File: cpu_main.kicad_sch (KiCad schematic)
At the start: 18 parts, among them Q1 9018G, U1 Z80, U2 74LS244, U21 2764, U3 74LS257, U4 74LS257, U5 74LS00, U6 27128, U7 27128/27256, U8 GA1, U9 74LS273

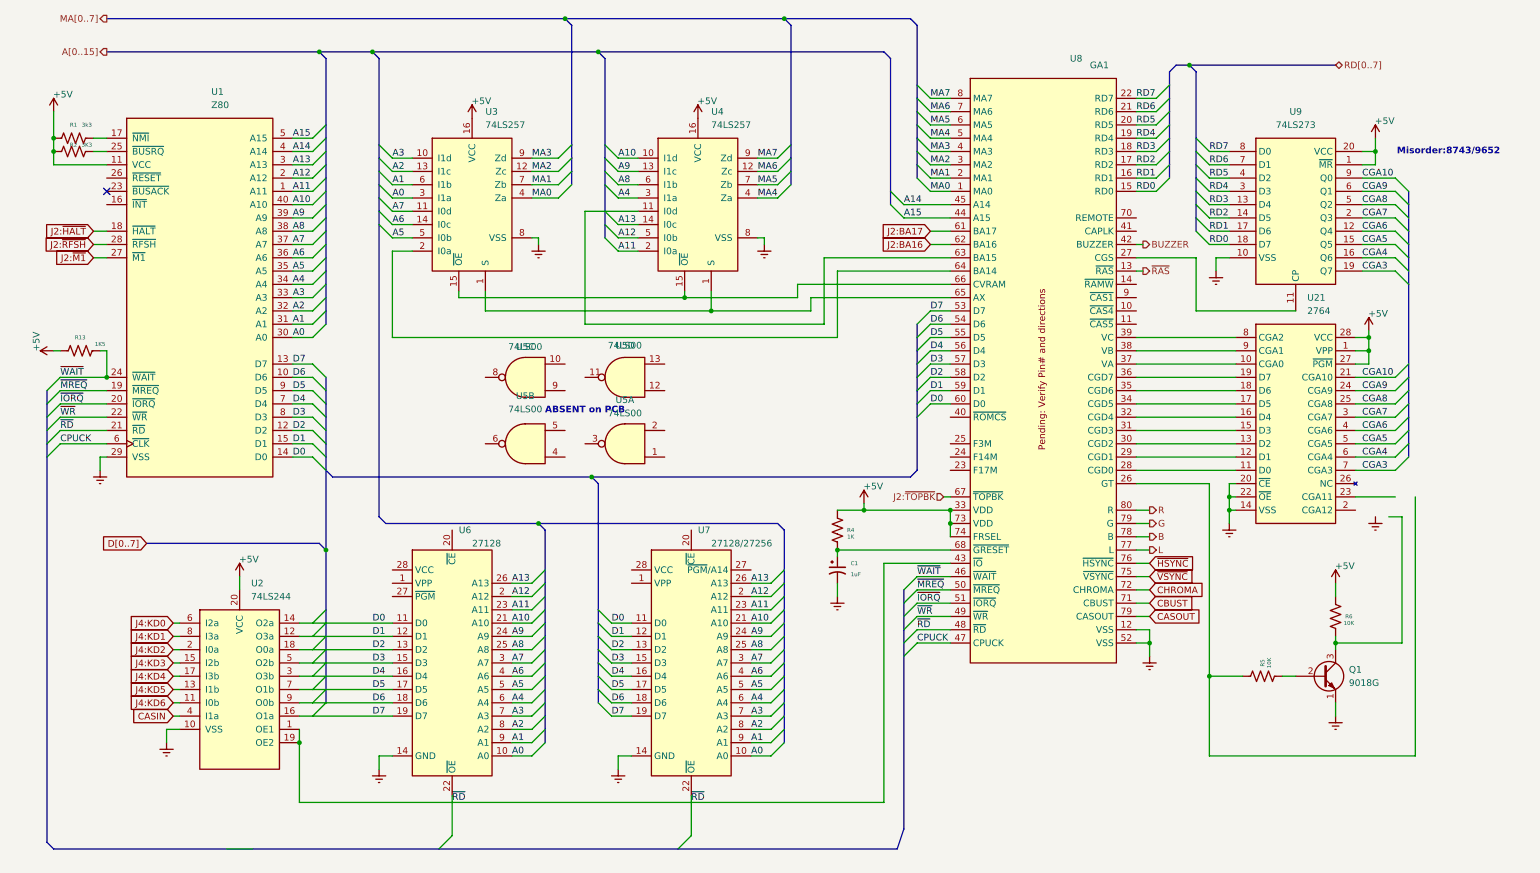
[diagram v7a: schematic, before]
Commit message: More updates on Top and Main diagrams
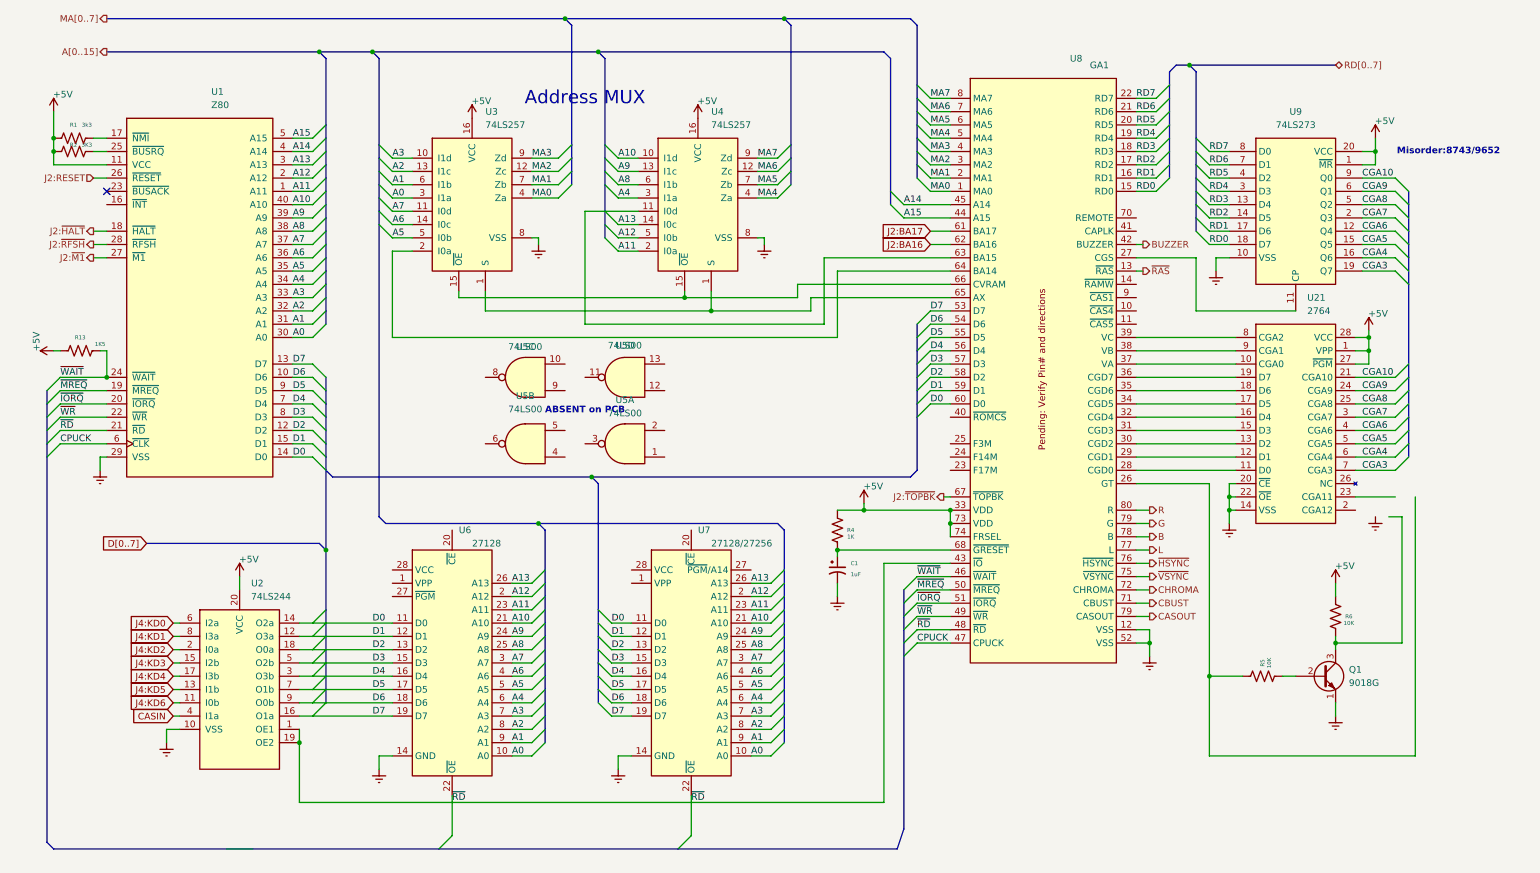
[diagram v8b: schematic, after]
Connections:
- net J2:RESET: now reaches U1.26 (~{RESET})
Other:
- note added: "Address MUX"
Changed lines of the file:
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@@
 		)
 	)
+	(wire
+		(pts
+			(xy 25.4 46.99) (xy 27.94 46.99)
+		)
+		(stroke
+			(width 0)
+			(type default)
+		)
+	)
 	(bus
 		(pts
@@
 		)
 	)
+	(text "Address MUX"
+		(exclude_from_sim no)
+		(at 119.38 31.75 0)
+		(effects
+			(font
+				(size 2.54 2.54)
+			)
+		)
+	)
 	(text "Misorder:8743/9652"
 		(exclude_from_sim no)
@@
 		)
 	)
-	(global_label "CBUST"
+	(global_label "D[0..7]"
 		(shape input)
-		(at 227.33 128.27 0)
+		(at 35.56 116.84 180)
 		(fields_autoplaced yes)
 		(effects
@@
 				(size 1.27 1.27)
 			)
-			(justify left)
+			(justify right)
 		)
 		(property "Intersheetrefs" "${INTERSHEET_REFS}"
-			(at 236.3628 128.27 0)
+			(at 25.9828 116.84 0)
 			(effects
 				(font
 					(size 1.27 1.27)
 				)
-				(justify left)
+				(justify right)
 				(hide yes)
 			)
 		)
 	)
-	(global_label "D[0..7]"
+	(global_label "J4:KD3"
 		(shape input)
-		(at 35.56 116.84 180)
+		(at 40.64 139.7 180)
 		(fields_autoplaced yes)
 		(effects
@@
 		)
 		(property "Intersheetrefs" "${INTERSHEET_REFS}"
-			(at 25.9828 116.84 0)
+			(at 31.1234 139.7 0)
 			(effects
 				(font
@@
 		)
 	)
-	(global_label "~{VSYNC}"
+	(global_label "J2:BA17"
 		(shape input)
-		(at 227.33 123.19 0)
+		(at 185.42 57.15 180)
 		(fields_autoplaced yes)
 		(effects
@@
 				(size 1.27 1.27)
 			)
-			(justify left)
+			(justify right)
 		)
 		(property "Intersheetrefs" "${INTERSHEET_REFS}"
-			(at 236.3024 123.19 0)
+			(at 174.8753 57.15 0)
 			(effects
 				(font
 					(size 1.27 1.27)
 				)
-				(justify left)
+				(justify right)
 				(hide yes)
 			)
 		)
 	)
-	(global_label "J2:~{HALT}"
+	(global_label "J4:KD2"
 		(shape input)
-		(at 25.4 57.15 180)
+		(at 40.64 137.16 180)
 		(fields_autoplaced yes)
 		(effects
@@
 		)
 		(property "Intersheetrefs" "${INTERSHEET_REFS}"
-			(at 15.2181 57.15 0)
+			(at 31.1234 137.16 0)
 			(effects
 				(font
@@
 		)
 	)
-	(global_label "J4:KD3"
+	(global_label "J4:KD5"
 		(shape input)
-		(at 40.64 139.7 180)
+		(at 40.64 144.78 180)
 		(fields_autoplaced yes)
 		(effects
@@
 		)
 		(property "Intersheetrefs" "${INTERSHEET_REFS}"
-			(at 31.1234 139.7 0)
+			(at 31.1234 144.78 0)
 			(effects
 				(font
@@
 		)
 	)
-	(global_label "J2:BA17"
+	(global_label "J4:KD6"
 		(shape input)
-		(at 185.42 57.15 180)
+		(at 40.64 147.32 180)
 		(fields_autoplaced yes)
 		(effects
@@
 		)
 		(property "Intersheetrefs" "${INTERSHEET_REFS}"
-			(at 174.8753 57.15 0)
+			(at 31.1234 147.32 0)
 			(effects
 				(font
@@
 		)
 	)
-	(global_label "J2:~{M1}"
+	(global_label "J4:KD0"
 		(shape input)
-		(at 25.4 62.23 180)
+		(at 40.64 132.08 180)
 		(fields_autoplaced yes)
 		(effects
@@
 		)
 		(property "Intersheetrefs" "${INTERSHEET_REFS}"
-			(at 16.972 62.23 0)
+			(at 31.1234 132.08 0)
 			(effects
 				(font
@@
 		)
 	)
-	(global_label "J4:KD2"
+	(global_label "J2:BA16"
 		(shape input)
-		(at 40.64 137.16 180)
+		(at 185.42 59.69 180)
 		(fields_autoplaced yes)
 		(effects
@@
 		)
 		(property "Intersheetrefs" "${INTERSHEET_REFS}"
-			(at 31.1234 137.16 0)
+			(at 174.8753 59.69 0)
 			(effects
 				(font
@@
 		)
 	)
-	(global_label "J4:KD5"
+	(global_label "J4:KD1"
 		(shape input)
-		(at 40.64 144.78 180)
+		(at 40.64 134.62 180)
 		(fields_autoplaced yes)
 		(effects
@@
 		)
 		(property "Intersheetrefs" "${INTERSHEET_REFS}"
-			(at 31.1234 144.78 0)
+			(at 31.1234 134.62 0)
 			(effects
 				(font
@@
 		)
 	)
-	(global_label "J4:KD6"
+	(global_label "CASIN"
 		(shape input)
-		(at 40.64 147.32 180)
+		(at 40.64 149.86 180)
 		(fields_autoplaced yes)
 		(effects
@@
 		)
 		(property "Intersheetrefs" "${INTERSHEET_REFS}"
-			(at 31.1234 147.32 0)
+			(at 32.1514 149.86 0)
 			(effects
 				(font
@@
 		)
 	)
-	(global_label "J4:KD0"
+	(global_label "J4:KD4"
 		(shape input)
-		(at 40.64 132.08 180)
+		(at 40.64 142.24 180)
 		(fields_autoplaced yes)
 		(effects
@@
 		)
 		(property "Intersheetrefs" "${INTERSHEET_REFS}"
-			(at 31.1234 132.08 0)
+			(at 31.1234 142.24 0)
 			(effects
 				(font
@@
 		)
 	)
-	(global_label "CASOUT"
-		(shape input)
-		(at 227.33 130.81 0)
+	(hierarchical_label "L"
+		(shape output)
+		(at 227.33 118.11 0)
 		(fields_autoplaced yes)
 		(effects
@@
 			(justify left)
 		)
-		(property "Intersheetrefs" "${INTERSHEET_REFS}"
-			(at 237.5119 130.81 0)
-			(effects
-				(font
-					(size 1.27 1.27)
-				)
-				(justify left)
-				(hide yes)
-			)
-		)
 	)
-	(global_label "J2:~{RFSH}"
-		(shape input)
+	(hierarchical_label "J2:~{RFSH}"
+		(shape output)
 		(at 25.4 59.69 180)
 		(fields_autoplaced yes)
@@
 			(justify right)
 		)
-		(property "Intersheetrefs" "${INTERSHEET_REFS}"
-			(at 14.7343 59.69 0)
-			(effects
-				(font
-					(size 1.27 1.27)
-				)
-				(justify right)
-				(hide yes)
-			)
-		)
 	)
-	(global_label "~{HSYNC}"
-		(shape input)
-		(at 227.33 120.65 0)
+	(hierarchical_label "~{VSYNC}"
+		(shape output)
+		(at 227.33 123.19 0)
 		(fields_autoplaced yes)
 		(effects
@@
 			(justify left)
 		)
-		(property "Intersheetrefs" "${INTERSHEET_REFS}"
-			(at 236.5443 120.65 0)
-			(effects
-				(font
-					(size 1.27 1.27)
-				)
-				(justify left)
-				(hide yes)
-			)
-		)
 	)
-	(global_label "J2:BA16"
-		(shape input)
-		(at 185.42 59.69 180)
+	(hierarchical_label "J2:~{M1}"
+		(shape output)
+		(at 25.4 62.23 180)
 		(fields_autoplaced yes)
 		(effects
@@
 			(justify right)
 		)
-		(property "Intersheetrefs" "${INTERSHEET_REFS}"
-			(at 174.8753 59.69 0)
-			(effects
-				(font
-					(size 1.27 1.27)
-				)
-				(justify right)
-				(hide yes)
-			)
-		)
 	)
-	(global_label "J4:KD1"
-		(shape input)
-		(at 40.64 134.62 180)
+	(hierarchical_label "J2:~{HALT}"
+		(shape output)
+		(at 25.4 57.15 180)
 		(fields_autoplaced yes)
 		(effects
@@
 			(justify right)
 		)
-		(property "Intersheetrefs" "${INTERSHEET_REFS}"
-			(at 31.1234 134.62 0)
-			(effects
-				(font
-					(size 1.27 1.27)
-				)
-				(justify right)
-				(hide yes)
-			)
-		)
 	)
-	(global_label "CASIN"
-		(shape input)
-		(at 40.64 149.86 180)
+	(hierarchical_label "CASOUT"
+		(shape output)
+		(at 227.33 130.81 0)
 		(fields_autoplaced yes)
 		(effects
@@
 				(size 1.27 1.27)
 			)
-			(justify right)
-		)
-		(property "Intersheetrefs" "${INTERSHEET_REFS}"
-			(at 32.1514 149.86 0)
-			(effects
-				(font
-					(size 1.27 1.27)
-				)
-				(justify right)
-				(hide yes)
-			)
+			(justify left)
 		)
 	)
-	(global_label "CHROMA"
-		(shape input)
+	(hierarchical_label "CHROMA"
+		(shape output)
 		(at 227.33 125.73 0)
 		(fields_autoplaced yes)
@@
 			(justify left)
 		)
-		(property "Intersheetrefs" "${INTERSHEET_REFS}"
-			(at 238.0562 125.73 0)
-			(effects
-				(font
-					(size 1.27 1.27)
-				)
-				(justify left)
-				(hide yes)
-			)
-		)
 	)
-	(global_label "J4:KD4"
-		(shape input)
-		(at 40.64 142.24 180)
+	(hierarchical_label "~{HSYNC}"
+		(shape output)
+		(at 227.33 120.65 0)
 		(fields_autoplaced yes)
 		(effects
@@
 				(size 1.27 1.27)
 			)
-			(justify right)
-		)
-		(property "Intersheetrefs" "${INTERSHEET_REFS}"
-			(at 31.1234 142.24 0)
-			(effects
-				(font
-					(size 1.27 1.27)
-				)
-				(justify right)
-				(hide yes)
-			)
+			(justify left)
 		)
 	)
-	(hierarchical_label "L"
+	(hierarchical_label "B"
 		(shape output)
-		(at 227.33 118.11 0)
+		(at 227.33 115.57 0)
 		(fields_autoplaced yes)
 		(effects
@@
 		)
 	)
-	(hierarchical_label "B"
+	(hierarchical_label "R"
 		(shape output)
-		(at 227.33 115.57 0)
+		(at 227.33 110.49 0)
 		(fields_autoplaced yes)
 		(effects
@@
 		)
 	)
-	(hierarchical_label "R"
-		(shape output)
-		(at 227.33 110.49 0)
+	(hierarchical_label "J2:RESET"
+		(shape input)
+		(at 25.4 46.99 180)
 		(fields_autoplaced yes)
 		(effects
@@
 				(size 1.27 1.27)
 			)
-			(justify left)
+			(justify right)
 		)
 	)
@@
 		)
 	)
+	(hierarchical_label "CBUST"
+		(shape output)
+		(at 227.33 128.27 0)
+		(fields_autoplaced yes)
+		(effects
+			(font
+				(size 1.27 1.27)
+			)
+			(justify left)
+		)
+	)
 	(hierarchical_label "J2:~{TOPBK}"
-		(shape input)
+		(shape output)
 		(at 187.96 107.95 180)
 		(fields_autoplaced yes)
